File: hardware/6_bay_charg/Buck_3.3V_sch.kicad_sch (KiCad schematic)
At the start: 13 parts, among them U1 TPS562200

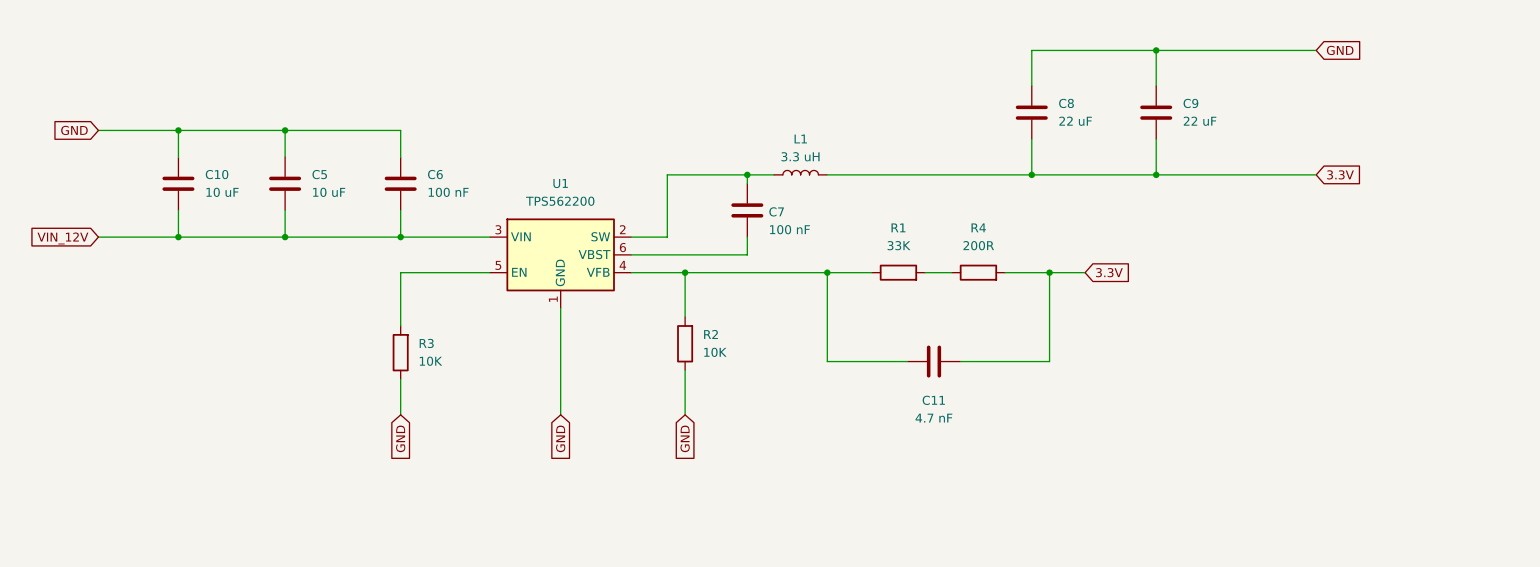
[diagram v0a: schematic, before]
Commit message: Update KiCad schematics: dual GPIO charge/discharge per bay
- Refactored bay power control logic
- Separated GPIOs for charge and discharge paths
- Added safe idle state with hardware interlock
- Improved overall safety and control clarity
- Updated and exported schematic PDF plots
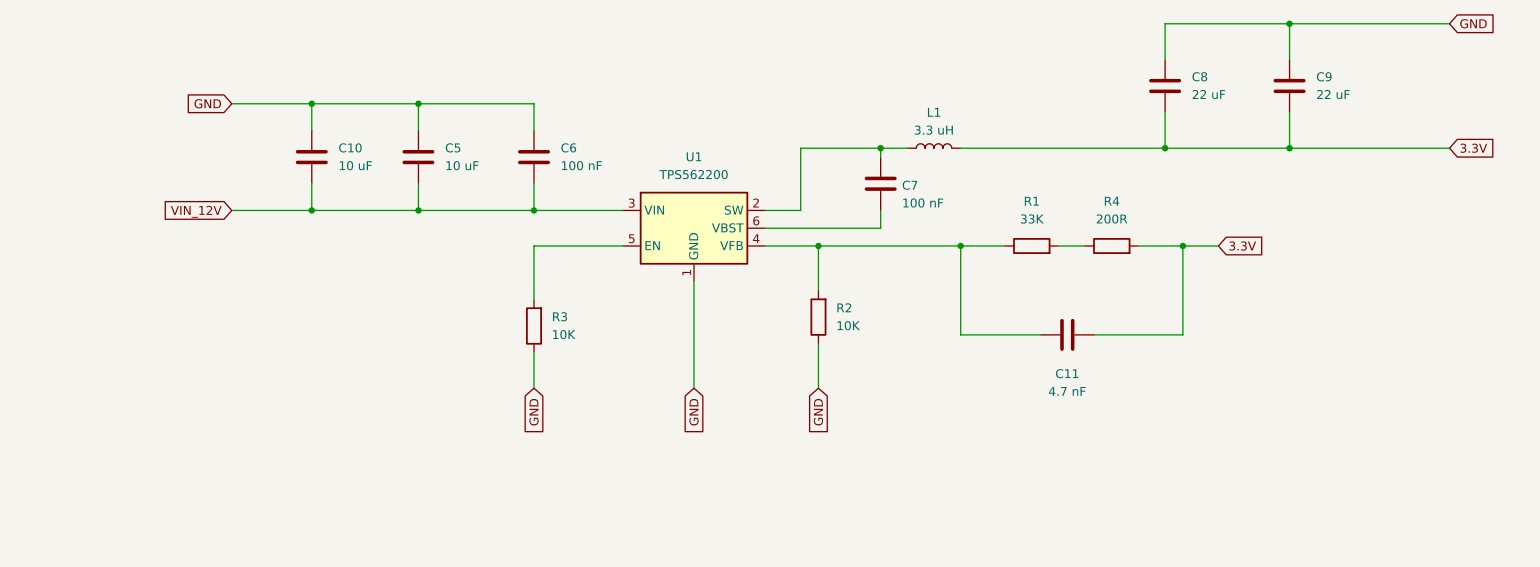
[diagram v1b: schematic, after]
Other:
- moved on the sheet: C10, C11, C5, C6, C7, C8, C9, L1, R1, R2, R3, R4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

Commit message: Integrate fan, USB interface, firmware, and cleaned KiCad schematics
- Added 12V fan for thermal management
- Integrated USB interface (hardware and firmware)
- Added initial firmware implementation
- Cleaned and refactored KiCad schematics
- Updated and regenerated schematic PDF plots
- Updated project README to reflect latest architecture
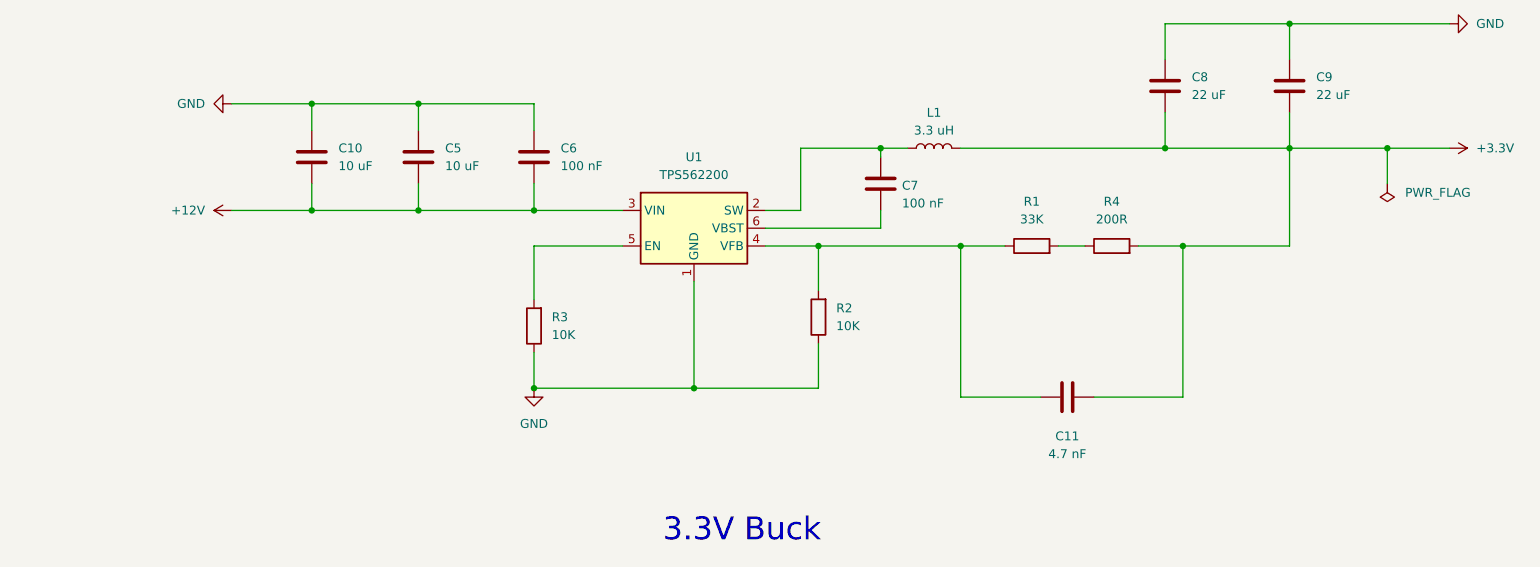
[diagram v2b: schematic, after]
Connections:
- net 3.3V renamed +3.3V
- net VIN_12V renamed +12V
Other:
- note added: "3.3V Buck"
- moved on the sheet: C11

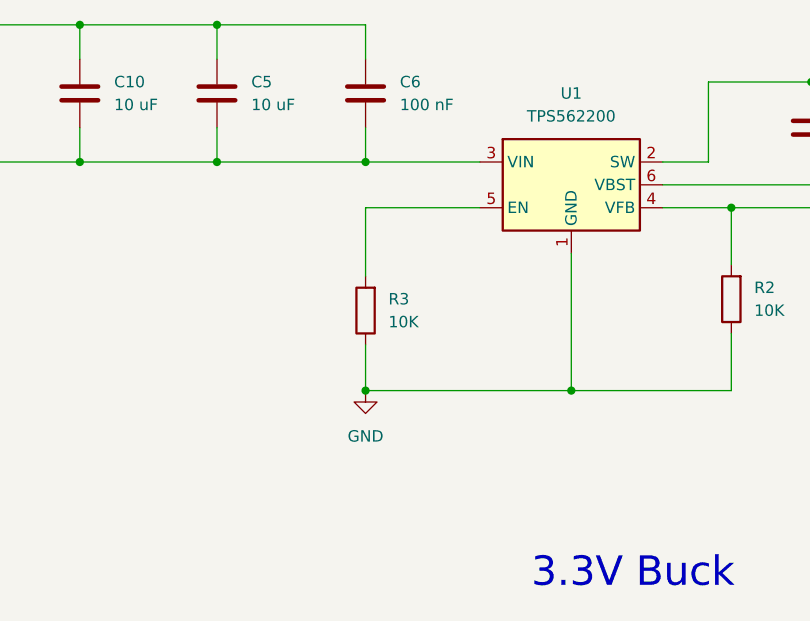
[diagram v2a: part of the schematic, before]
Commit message: Fixing Buck_3.3V  EN
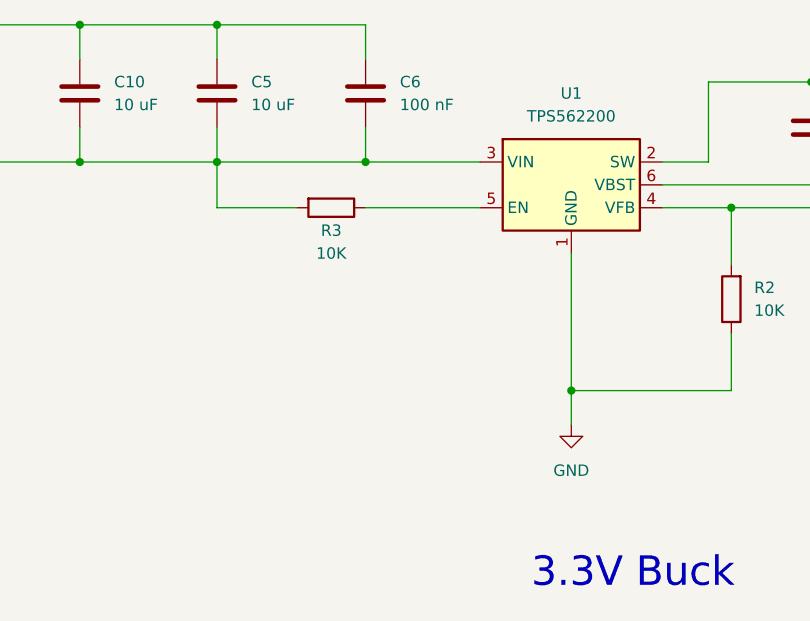
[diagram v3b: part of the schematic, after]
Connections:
- net +12V: now also R3.2
- net GND: no longer R3.1
- net at U1.5 (EN): now also R3.1; no longer R3.2
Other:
- moved on the sheet: R3
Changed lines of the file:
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@@
-	)
-	(junction
-		(at 116.84 110.49)
-		(diameter 0)
-		(color 0 0 0 0)
 	)
 	(junction
@@
 	(wire
 		(pts
-			(xy 116.84 105.41) (xy 116.84 110.49)
-		)
-		(stroke
-			(width 0)
-			(type default)
-		)
-	)
-	(wire
-		(pts
 			(xy 166.37 85.09) (xy 166.37 87.63)
 		)
@@
 	(wire
 		(pts
-			(xy 116.84 90.17) (xy 116.84 97.79)
-		)
-		(stroke
-			(width 0)
-			(type default)
-		)
-	)
-	(wire
-		(pts
 			(xy 154.94 76.2) (xy 166.37 76.2)
 		)
@@
 	(wire
 		(pts
-			(xy 116.84 110.49) (xy 139.7 110.49)
+			(xy 139.7 114.3) (xy 139.7 110.49)
+		)
+		(stroke
+			(width 0)
+			(type default)
+		)
+	)
+	(wire
+		(pts
+			(xy 100.33 90.17) (xy 100.33 85.09)
 		)
 		(stroke
@@
 		(pts
 			(xy 73.66 85.09) (xy 85.09 85.09)
+		)
+		(stroke
+			(width 0)
+			(type default)
+		)
+	)
+	(wire
+		(pts
+			(xy 109.22 90.17) (xy 100.33 90.17)
 		)
 		(stroke
@@
 	(symbol
 		(lib_id "power:GND")
-		(at 116.84 110.49 0)
+		(at 139.7 114.3 0)
 		(unit 1)
 		(exclude_from_sim no)
@@
 		(fields_autoplaced yes)
 		(property "Reference" "#PWR045"
-			(at 116.84 116.84 0)
+			(at 139.7 120.65 0)
 			(effects
 				(font
@@
 		)
 		(property "Value" "GND"
-			(at 116.84 115.57 0)
+			(at 139.7 119.38 0)
 			(effects
 				(font
@@
 		)
 		(property "Footprint" ""
-			(at 116.84 110.49 0)
+			(at 139.7 114.3 0)
 			(effects
 				(font
@@
 		)
 		(property "Datasheet" ""
-			(at 116.84 110.49 0)
+			(at 139.7 114.3 0)
 			(effects
 				(font
@@
 		)
 		(property "Description" "Power symbol creates a global label with name \"GND\" , ground"
-			(at 116.84 110.49 0)
+			(at 139.7 114.3 0)
 			(effects
 				(font
@@
 	(symbol
 		(lib_id "Device:R")
-		(at 116.84 101.6 180)
+		(at 113.03 90.17 270)
 		(unit 1)
 		(exclude_from_sim no)
@@
 		(on_board yes)
 		(dnp no)
-		(fields_autoplaced yes)
 		(property "Reference" "R3"
-			(at 119.38 100.3299 0)
-			(effects
-				(font
-					(size 1.27 1.27)
-				)
-				(justify right)
+			(at 113.03 92.71 90)
+			(effects
+				(font
+					(size 1.27 1.27)
+				)
 			)
 		)
 		(property "Value" "10K"
-			(at 119.38 102.8699 0)
-			(effects
-				(font
-					(size 1.27 1.27)
-				)
-				(justify right)
+			(at 113.03 95.25 90)
+			(effects
+				(font
+					(size 1.27 1.27)
+				)
 			)
 		)
 		(property "Footprint" ""
-			(at 118.618 101.6 90)
+			(at 113.03 88.392 90)
 			(effects
 				(font
@@
 		)
 		(property "Datasheet" "~"
-			(at 116.84 101.6 0)
+			(at 113.03 90.17 0)
 			(effects
 				(font
@@
 		)
 		(property "Description" "Resistor"
-			(at 116.84 101.6 0)
-			(effects
-				(font
+			(at 113.03 90.17 0)
+			(effects
+				(font
